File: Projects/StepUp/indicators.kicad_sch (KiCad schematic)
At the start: 10 parts, among them Q7 2N7002-7-F

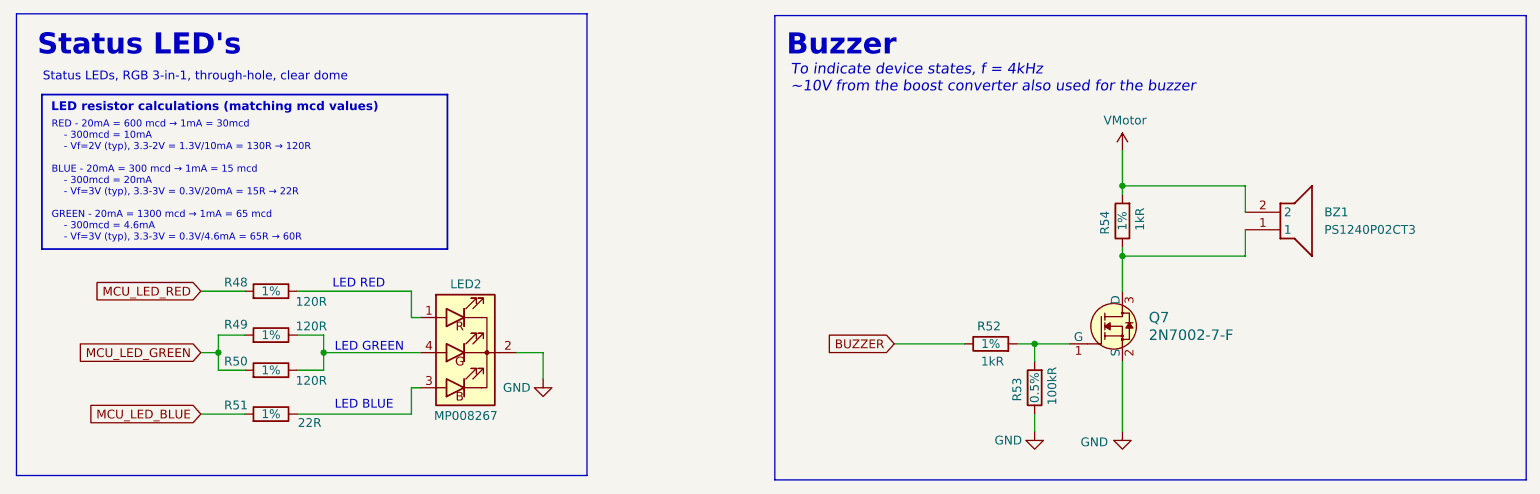
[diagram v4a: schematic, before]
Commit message: feat(v0.3): Minor updates for PCBWay order
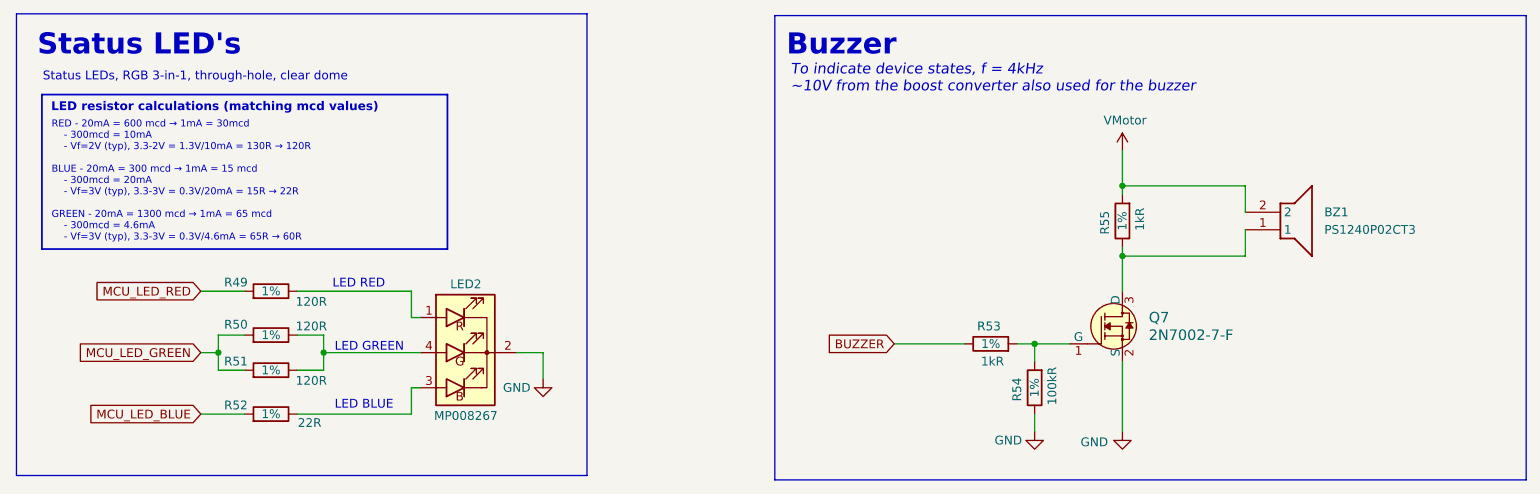
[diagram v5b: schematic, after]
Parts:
- BZ1: now left out of the parts list
- LED2: Manufacturer (none) -> Multicomp Pro; Manufacturer Part Number (none) -> MP008267; Manufacturer_Name Multicomp Pro -> (none); Manufacturer_Part_Number MP008267 -> (none); now left out of the parts list
- R54: renamed from R53; MPN RT0603DRE10100KL -> RC0603FR-07100RL; Tolerance 0.5% -> 1%
- renumbered R48 to R49, R49 to R50, R50 to R51, R51 to R52, R52 to R53, R54 to R55
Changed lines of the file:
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@@
 		(on_board yes)
 		(dnp no)
-		(property "Reference" "R53"
+		(property "Reference" "R54"
 			(at 185.42 113.284 90)
 			(effects
@@
 			)
 		)
-		(property "Tolerance" "0.5%"
+		(property "Tolerance" "1%"
 			(at 187.96 113.03 90)
 			(effects
@@
 			)
 		)
-		(property "MPN" "RT0603DRE10100KL"
+		(property "MPN" "RC0603FR-07100RL"
 			(at 187.96 113.03 0)
 			(effects
@@
 			(project "StepUp"
 				(path "/e0cca1c7-c263-49eb-8c40-74000ebe5285/9dda156e-3fdf-45bb-95f8-ac79c3ca0e44"
-					(reference "R53")
+					(reference "R54")
 					(unit 1)
 				)
@@
 		(unit 1)
 		(exclude_from_sim no)
-		(in_bom yes)
+		(in_bom no)
 		(on_board yes)
 		(dnp no)
@@
 		(on_board yes)
 		(dnp no)
-		(property "Reference" "R48"
+		(property "Reference" "R49"
 			(at 72.39 97.79 90)
 			(effects
@@
 			(project "StepUp"
 				(path "/e0cca1c7-c263-49eb-8c40-74000ebe5285/9dda156e-3fdf-45bb-95f8-ac79c3ca0e44"
-					(reference "R48")
+					(reference "R49")
 					(unit 1)
 				)
@@
 		(on_board yes)
 		(dnp no)
-		(property "Reference" "R51"
+		(property "Reference" "R52"
 			(at 72.39 115.57 90)
 			(effects
@@
 			(project "StepUp"
 				(path "/e0cca1c7-c263-49eb-8c40-74000ebe5285/9dda156e-3fdf-45bb-95f8-ac79c3ca0e44"
-					(reference "R51")
+					(reference "R52")
 					(unit 1)
 				)
@@
 		(on_board yes)
 		(dnp no)
-		(property "Reference" "#PWR095"
+		(property "Reference" "#PWR096"
 			(at 116.84 118.11 0)
 			(effects
@@
 			(project "StepUp"
 				(path "/e0cca1c7-c263-49eb-8c40-74000ebe5285/9dda156e-3fdf-45bb-95f8-ac79c3ca0e44"
-					(reference "#PWR095")
+					(reference "#PWR096")
 					(unit 1)
 				)
@@
 		(on_board yes)
 		(dnp no)
-		(property "Reference" "R54"
+		(property "Reference" "R55"
 			(at 198.12 89.154 90)
 			(effects
@@
 			(project "StepUp"
 				(path "/e0cca1c7-c263-49eb-8c40-74000ebe5285/9dda156e-3fdf-45bb-95f8-ac79c3ca0e44"
-					(reference "R54")
+					(reference "R55")
 					(unit 1)
 				)
@@
 		(on_board yes)
 		(dnp no)
-		(property "Reference" "R52"
+		(property "Reference" "R53"
 			(at 181.356 104.14 90)
 			(effects
@@
 			(project "StepUp"
 				(path "/e0cca1c7-c263-49eb-8c40-74000ebe5285/9dda156e-3fdf-45bb-95f8-ac79c3ca0e44"
-					(reference "R52")
+					(reference "R53")
 					(unit 1)
 				)
@@
 		(on_board yes)
 		(dnp no)
-		(property "Reference" "R49"
+		(property "Reference" "R50"
 			(at 72.39 103.886 90)
 			(effects
@@
 			(project "StepUp"
 				(path "/e0cca1c7-c263-49eb-8c40-74000ebe5285/9dda156e-3fdf-45bb-95f8-ac79c3ca0e44"
-					(reference "R49")
+					(reference "R50")
 					(unit 1)
 				)
@@
 		(on_board yes)
 		(dnp no)
-		(property "Reference" "#PWR096"
+		(property "Reference" "#PWR097"
 			(at 187.96 125.73 0)
 			(effects
@@
 			(project "StepUp"
 				(path "/e0cca1c7-c263-49eb-8c40-74000ebe5285/9dda156e-3fdf-45bb-95f8-ac79c3ca0e44"
-					(reference "#PWR096")
+					(reference "#PWR097")
 					(unit 1)
 				)
@@
 		(on_board yes)
 		(dnp no)
-		(property "Reference" "#PWR098"
+		(property "Reference" "#PWR099"
 			(at 200.66 125.73 0)
 			(effects
@@
 			(project "StepUp"
 				(path "/e0cca1c7-c263-49eb-8c40-74000ebe5285/9dda156e-3fdf-45bb-95f8-ac79c3ca0e44"
-					(reference "#PWR098")
+					(reference "#PWR099")
 					(unit 1)
 				)
@@
 		(on_board yes)
 		(dnp no)
-		(property "Reference" "#PWR097"
+		(property "Reference" "#PWR098"
 			(at 200.66 82.55 0)
 			(effects
@@
 			(project "StepUp"
 				(path "/e0cca1c7-c263-49eb-8c40-74000ebe5285/9dda156e-3fdf-45bb-95f8-ac79c3ca0e44"
-					(reference "#PWR097")
+					(reference "#PWR098")
 					(unit 1)
 				)
@@
 		(unit 1)
 		(exclude_from_sim no)
-		(in_bom yes)
+		(in_bom no)
 		(on_board yes)
 		(dnp no)
@@
 			)
 		)
-		(property "Manufacturer_Name" "Multicomp Pro"
+		(property "Manufacturer" "Multicomp Pro"
 			(at 116.84 619.38 0)
 			(effects
@@
 			)
 		)
-		(property "Manufacturer_Part_Number" "MP008267"
+		(property "Manufacturer Part Number" "MP008267"
 			(at 116.84 719.38 0)
 			(effects
@@
 		(on_board yes)
 		(dnp no)
-		(property "Reference" "R50"
+		(property "Reference" "R51"
 			(at 72.39 109.22 90)
 			(effects
@@
 			(project "StepUp"
 				(path "/e0cca1c7-c263-49eb-8c40-74000ebe5285/9dda156e-3fdf-45bb-95f8-ac79c3ca0e44"
-					(reference "R50")
+					(reference "R51")
 					(unit 1)
 				)
